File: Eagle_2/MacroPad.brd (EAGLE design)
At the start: 56.8 x 57.1 mm, 41 parts, among them SW00 SWITCH-SMD-EVQP-P2602W, SW01 KEYSWITCH-PLAIN-MX-1U, SW02 KEYSWITCH-PLAIN-MX-1U, SW03 KEYSWITCH-PLAIN-MX-1U, SW04 KEYSWITCH-PLAIN-MX-1U, SW05 KEYSWITCH-PLAIN-MX-1U, SW06 KEYSWITCH-PLAIN-MX-1U, SW07 KEYSWITCH-PLAIN-MX-1U, SW08 KEYSWITCH-PLAIN-MX-1U, SW09 KEYSWITCH-PLAIN-MX-1U, SW10 KEYSWITCH-PLAIN-MX-1U, SW11 KEYSWITCH-PLAIN-MX-1U, SW12 KEYSWITCH-PLAIN-MX-1U

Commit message: Add top and bottom ground plane and merge gnd and ugnd
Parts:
- added C9: 0.1u, Components:C0603
- moved C3 1.35 mm to (4.19, 35.6)
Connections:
- removed net UGND: C1.1, C2.1, C3.2, C4.2, C5.2, C6.2, C7.2, C8.2, R2.1, SW00.1A, SW00.1B, U$1.15, U$1.23, U$1.35, U$1.43, U$1.5, U$1.TAB, USB1.GND, Y1.2, Y1.4
- net GND: now also C1.1, C2.1, C3.2, C4.2, C5.2, C6.2, C7.2, C8.2, C9.2, R2.1, SW00.1A, SW00.1B, U$1.15, U$1.23, U$1.35, U$1.43, U$1.5, U$1.TAB, USB1.GND, Y1.2, Y1.4
- net VCC: now also C9.1
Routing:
- net VCC: track 30.7 -> 82.4 mm, vias 4 -> 6
- net GND: track 0.00 -> 24.7 mm, vias 0 -> 7
- net N$3: track 8.76 -> 25.5 mm
- net UGND: track 16.3 -> 0.00 mm, vias 4 -> 0
- added copper zone on layer 1, net GND
- added copper zone on layer 16, net GND

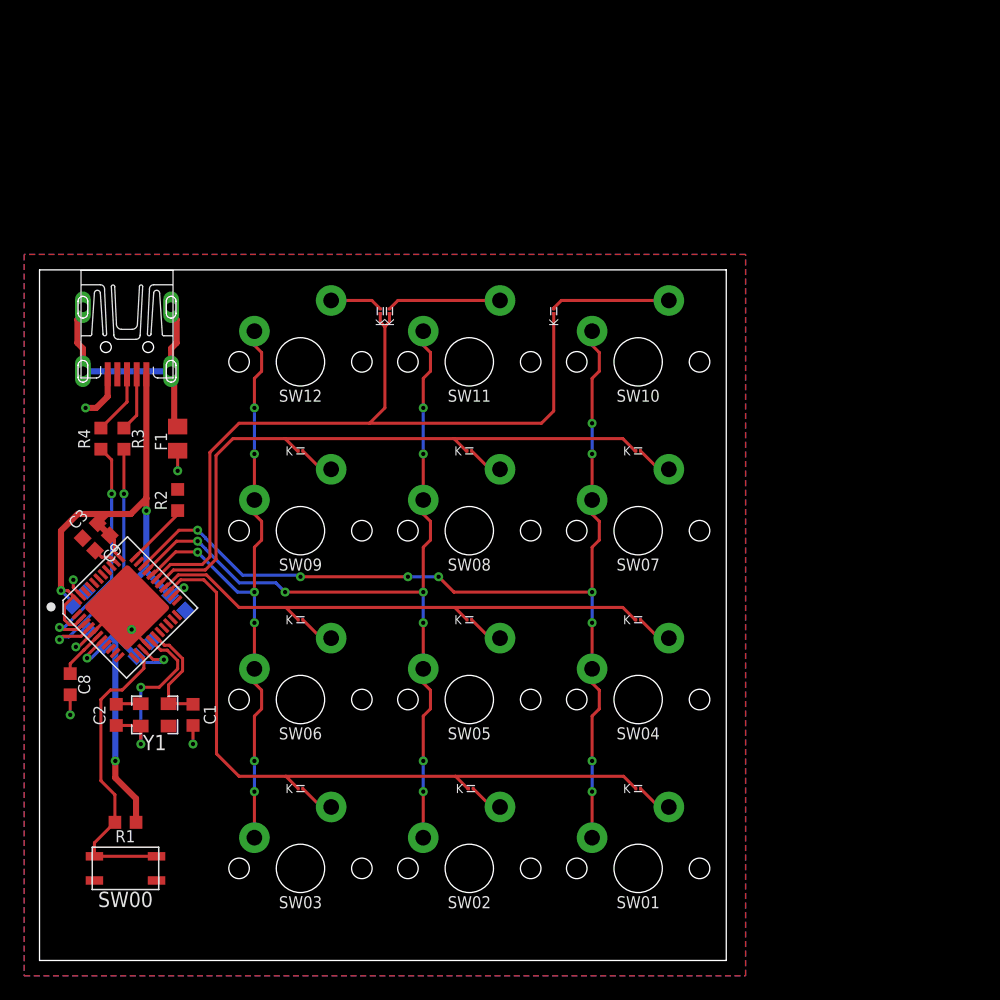
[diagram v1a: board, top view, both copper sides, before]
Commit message: Reduce acute angles and move vias farther from board
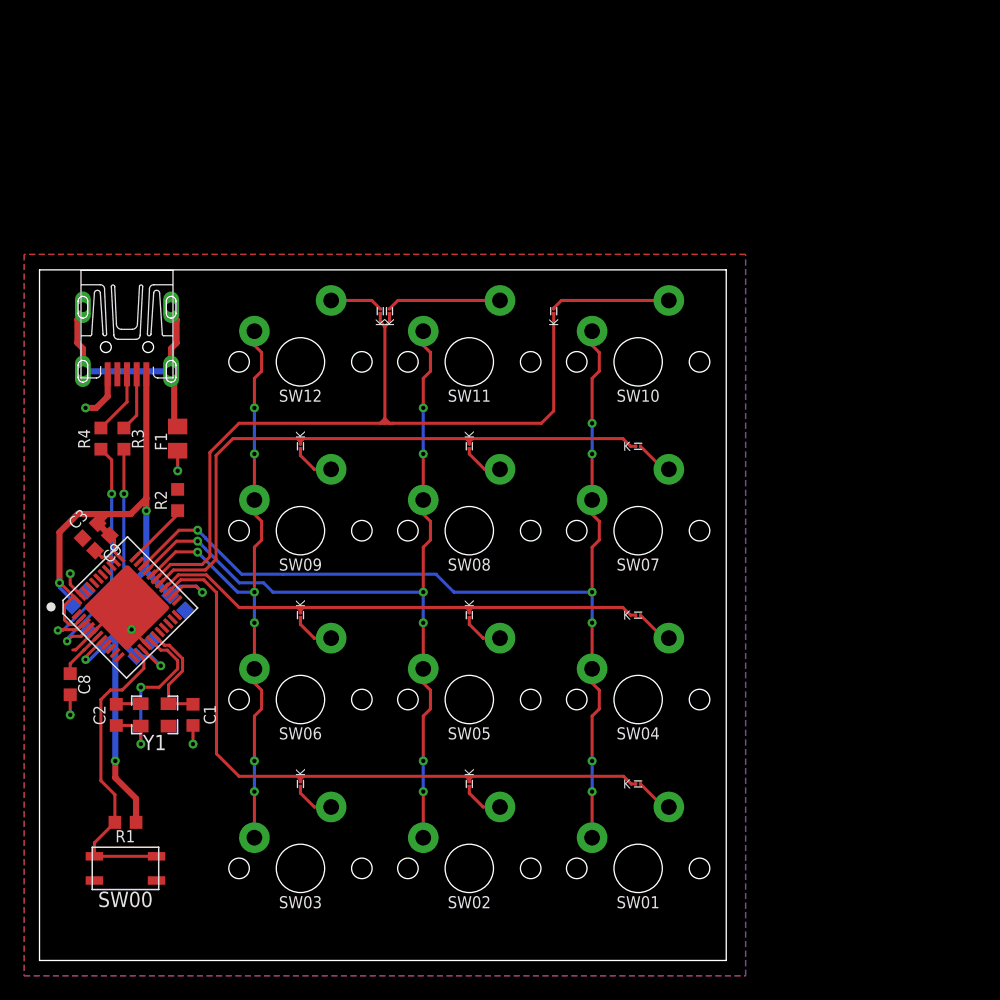
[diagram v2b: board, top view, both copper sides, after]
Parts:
- moved D2 0.40 mm to (35.6, 14.6), turned to 270 degrees
- moved D1 0.38 mm to (49.5, 14.6)
- moved D3 0.38 mm to (21.6, 14.6), turned to 270 degrees
- moved D4 0.38 mm to (49.5, 28.6)
- moved D5 0.38 mm to (35.6, 28.6), turned to 270 degrees
- moved D6 0.38 mm to (21.6, 28.6), turned to 270 degrees
- moved D7 0.38 mm to (49.5, 42.5)
- moved D8 0.38 mm to (35.6, 42.5), turned to 270 degrees
- moved D9 0.38 mm to (21.6, 42.5), turned to 270 degrees
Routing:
- net VCC: track 82.4 -> 86.5 mm
- net N$8: track 21.2 -> 20.2 mm
- net GND: track 24.7 -> 25.7 mm, vias 7 -> 6
- net N$12: track 2.85 -> 3.59 mm
- net N$24: track 2.98 -> 3.59 mm
- net N$21: track 2.98 -> 3.59 mm
- net N$15: track 2.98 -> 3.59 mm
- net N$33: track 2.98 -> 3.59 mm
- net N$6: track 19.6 -> 20.1 mm
- net N$38: track 62.8 -> 63.4 mm
- net N$30: track 2.98 -> 3.51 mm
- net N$40: vias 8 -> 7
- net N$10: vias 10 -> 7

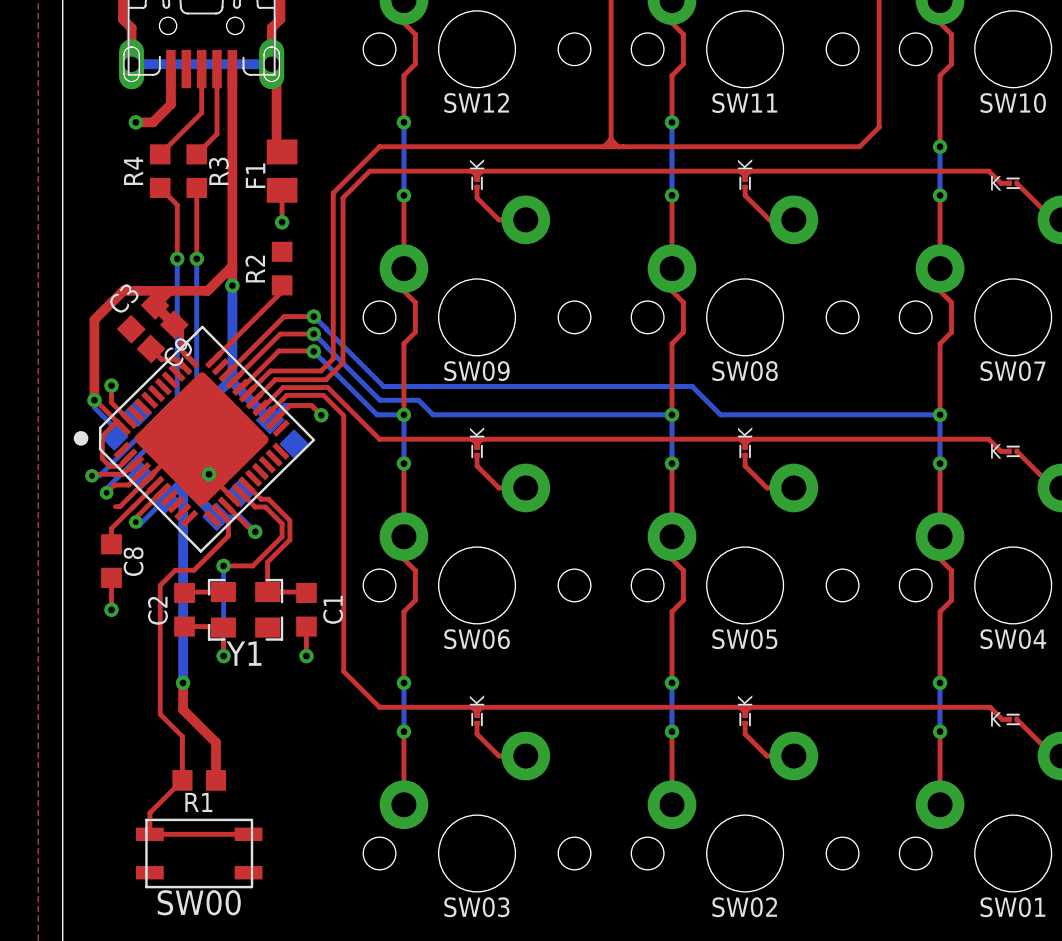
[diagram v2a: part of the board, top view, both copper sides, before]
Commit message: Align all labels
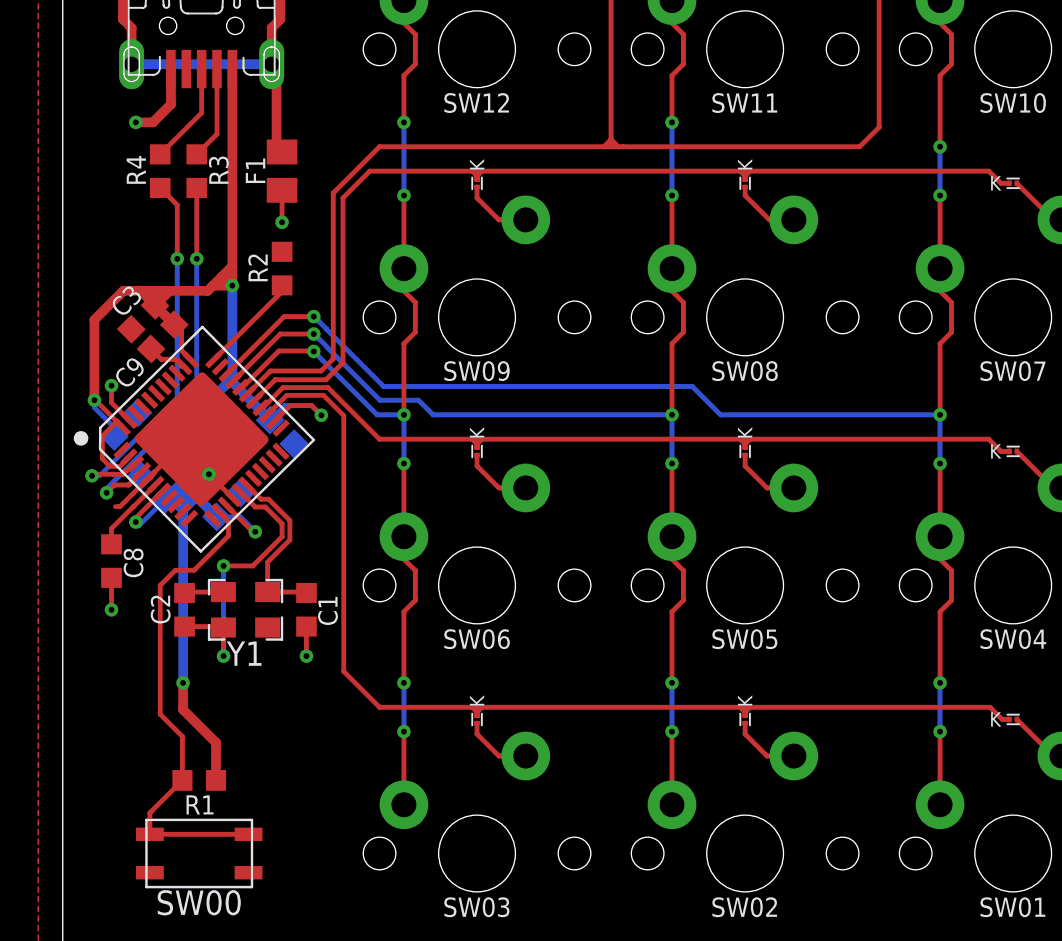
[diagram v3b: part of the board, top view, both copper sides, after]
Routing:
- net VCC: track 86.5 -> 94.7 mm

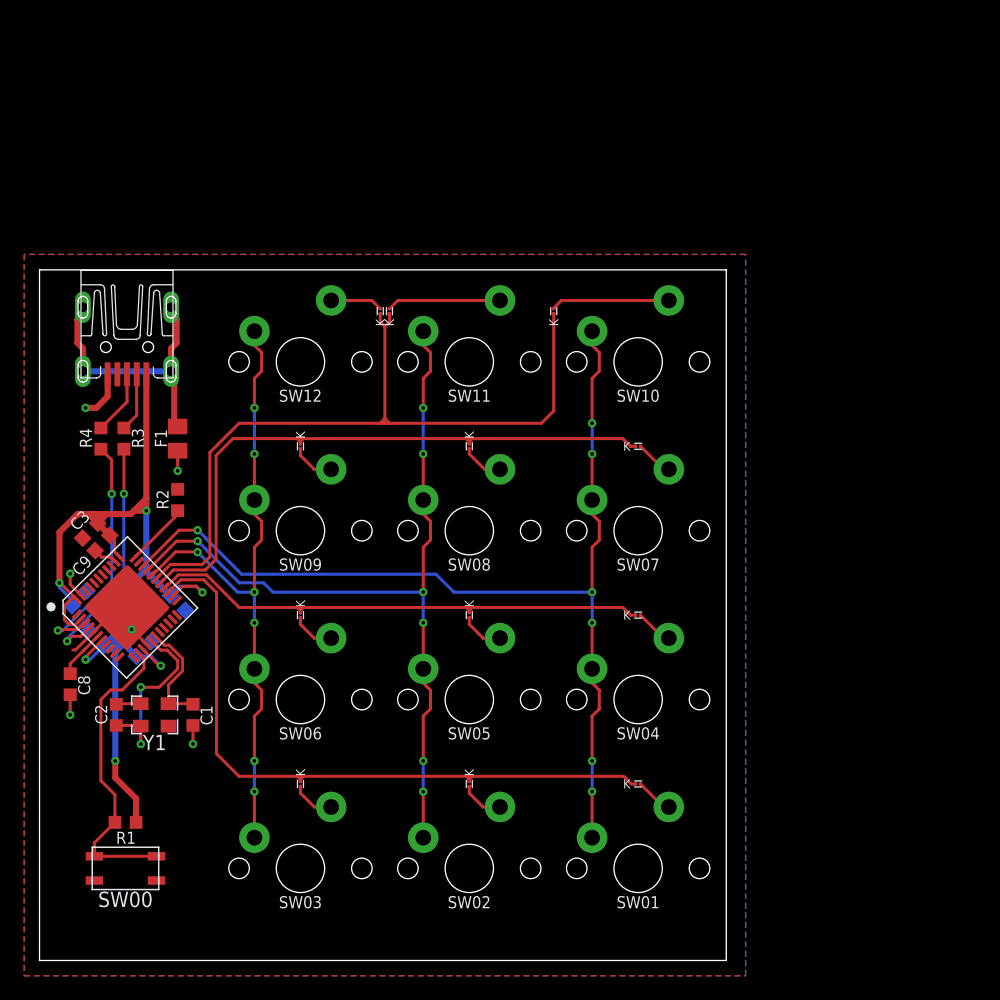
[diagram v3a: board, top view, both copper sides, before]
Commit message: Update layout with appropriate spacing between switches (100mil border)
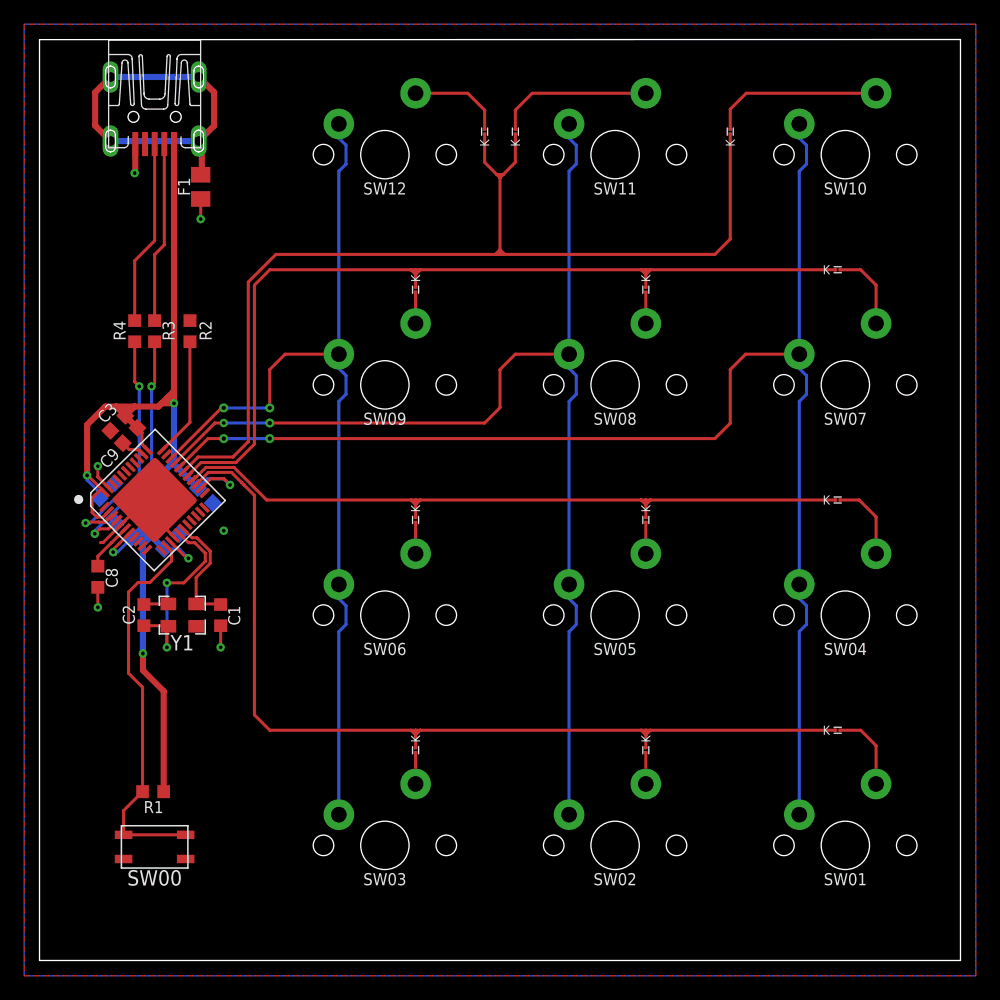
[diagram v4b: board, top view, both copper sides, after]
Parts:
- moved SW10 24.2 mm to (66.7, 66.7)
- moved D7 22.0 mm to (66.0, 57.1)
- moved SW07 21.0 mm to (66.7, 47.6)
- moved SW11 21.0 mm to (47.6, 66.7)
- moved F1 20.9 mm to (13.3, 64.0)
- moved D10 20.8 mm to (57.1, 68.6)
- moved D8 19.5 mm to (50.2, 55.5)
- moved USB1 19.2 mm to (9.53, 76.2)
- moved D4 19.1 mm to (66.0, 38.1)
- moved SW04 18.5 mm to (66.7, 28.6)
- moved SW12 18.5 mm to (28.6, 66.7)
- moved D11 18.1 mm to (39.4, 68.6)
- moved SW01 17.3 mm to (66.7, 9.53)
- moved D12 17.2 mm to (36.8, 68.6)
- moved D1 17.1 mm to (66.0, 19.1)
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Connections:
- net N$10: now also U$1.29; no longer U$1.31
- net N$16: now also U$1.31; no longer U$1.29
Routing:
- net N$10: track 83.9 -> 116.4 mm, vias 7 -> 2
- net N$40: track 69.0 -> 96.8 mm, vias 7 -> 2
- net N$16: track 54.1 -> 78.0 mm, vias 7 -> 2
- net N$38: track 63.4 -> 85.9 mm
- net N$14: track 56.6 -> 77.9 mm
- net N$32: track 52.3 -> 73.4 mm
- net VCC: track 94.7 -> 112.2 mm
- net N$26: track 43.5 -> 59.9 mm
- net N$7: track 4.88 -> 14.9 mm
- net N$5: track 5.34 -> 15.3 mm
- net N$3: track 25.5 -> 32.4 mm
- net N$11: track 23.4 -> 30.2 mm
- net N$4: track 5.36 -> 9.91 mm
- net N$36: track 9.85 -> 14.3 mm
- net N$27: track 3.14 -> 6.69 mm
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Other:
- board size 56.8 x 57.1 mm -> 76.2 x 76.2 mm
